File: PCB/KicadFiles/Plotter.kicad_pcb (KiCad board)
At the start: 2 copper layers, 1 part, among them U1 TMC2209-V1.2_Bigtreetech

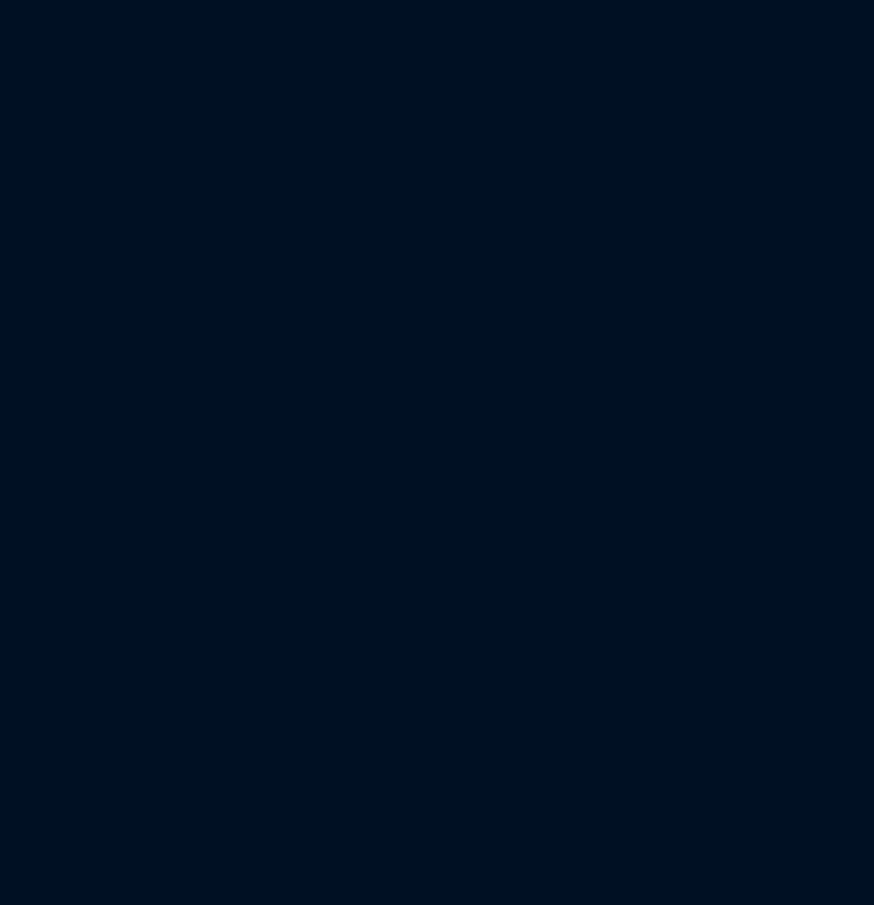
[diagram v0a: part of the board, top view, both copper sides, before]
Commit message: stall detect lauft
https://github.com/teemuatlut/TMCStepper/issues/178
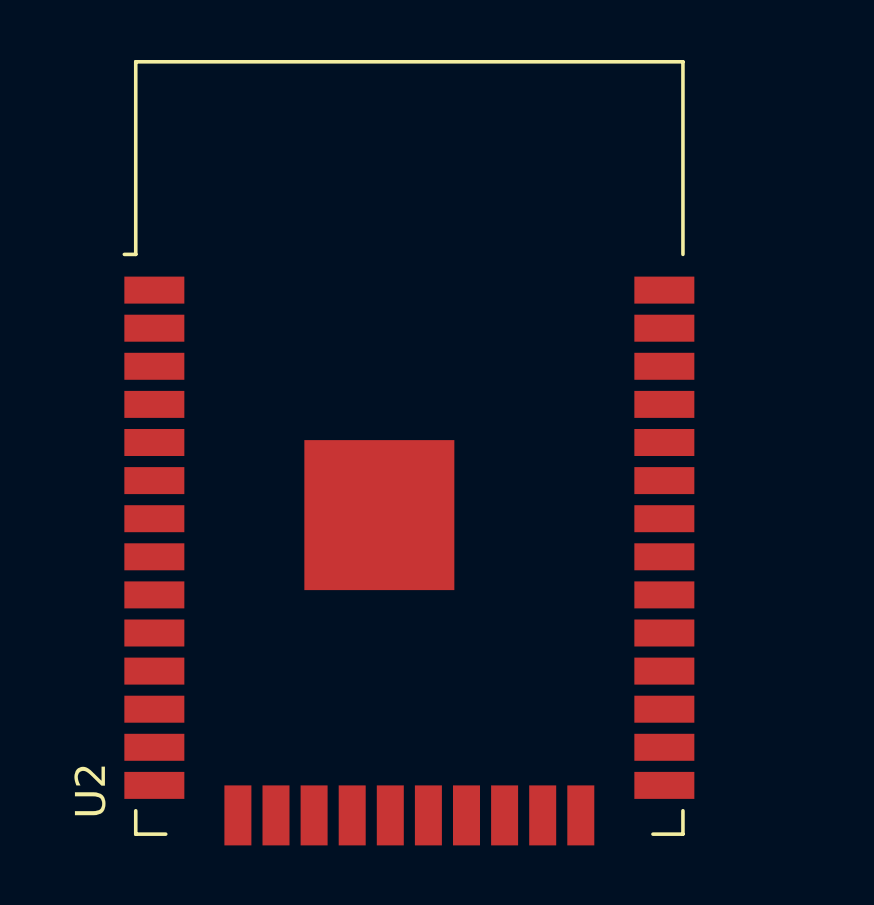
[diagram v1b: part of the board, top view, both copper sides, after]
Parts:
- added U2: ESP32-WROOM-32, RF_Module:ESP32-WROOM-32, F.Cu at (40.0, 70.0)

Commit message: schematic half way done
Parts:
- added C1: 100u, Capacitor_SMD:CP_Elec_6.3x7.7, F.Cu at (125.0, 65.0)
- added C2: 100u, Capacitor_SMD:CP_Elec_6.3x7.7, F.Cu at (131.2, 56.8)
- added C3: 100u, Capacitor_SMD:CP_Elec_6.3x7.7, F.Cu at (99.9, 96.2)
- added C4: C, Capacitor_SMD:C_0603_1608Metric, F.Cu at (87.7, 101.1)
- added C5: C, Capacitor_SMD:C_0603_1608Metric, F.Cu at (138.4, 59.5)
- added C6: 100u, Capacitor_SMD:CP_Elec_6.3x7.7, F.Cu at (143.1, 49.0)
- added D1: LED, LED_SMD:LED_0603_1608Metric, F.Cu at (138.4, 54.3)
- added D2: 10v, Package_TO_SOT_SMD:SOT-23, F.Cu at (111.6, 63.1)
- added D3: LED, LED_SMD:LED_0603_1608Metric, F.Cu at (138.4, 56.9)
- added D4: LED, LED_SMD:LED_0603_1608Metric, F.Cu at (116.1, 62.2)
- added D5: LED, LED_SMD:LED_0603_1608Metric, F.Cu at (116.1, 64.8)
- added F1: Fuse, Fuse:Fuseholder_Cylinder-5x20mm_Schurter_0031_8201_Horizontal_Open, F.Cu at (52.6, 85.6)
- added H1: MountingHole M3, MountingHole:MountingHole_3.2mm_M3_Pad_Via, F.Cu at (134.2, 64.8)
- added H2: MountingHole M3, MountingHole:MountingHole_3.2mm_M3_Pad_Via, F.Cu at (131.7, 73.0)
- added H3: MountingHole M3, MountingHole:MountingHole_3.2mm_M3_Pad_Via, F.Cu at (152.3, 48.9)
- added H4: MountingHole M3, MountingHole:MountingHole_3.2mm_M3_Pad_Via, F.Cu at (123.8, 73.0)
- added J1: JTAG, Connector_IDC:IDC-Header_2x10_P2.54mm_Vertical, F.Cu at (55.6, 51.0)
- added J2: DBG_UART, Connector_JST:JST_XH_B3B-XH-A_1x03_P2.50mm_Vertical, F.Cu at (68.2, 94.5)
- added J3: 12V IN, Connector_BarrelJack:BarrelJack_CLIFF_FC681465S_SMT_Horizontal, F.Cu at (118.2, 52.9)
- added J4: Motor LIN, Connector_JST:JST_XH_B4B-XH-A_1x04_P2.50mm_Vertical, F.Cu at (53.8, 94.5)
- added J5: Servo, Connector_JST:JST_XH_B3B-XH-A_1x03_P2.50mm_Vertical, F.Cu at (129.4, 48.2)
- added J6: Motor ROT, Connector_JST:JST_XH_B4B-XH-A_1x04_P2.50mm_Vertical, F.Cu at (95.3, 70.7)
- added Q1: SQJ479EP, Package_TO_SOT_SMD:TDSON-8-1, F.Cu at (54.4, 102.3)
- added R1: 100, Resistor_SMD:R_0603_1608Metric, F.Cu at (83.7, 101.1)
- added R10: 10k, Resistor_SMD:R_0603_1608Metric, F.Cu at (91.7, 103.6)
- added R11: 10k, Resistor_SMD:R_0603_1608Metric, F.Cu at (75.7, 104.1)
- added R12: 10k, Resistor_SMD:R_0603_1608Metric, F.Cu at (72.3, 78.7)
- added R13: 10k, Resistor_SMD:R_0603_1608Metric, F.Cu at (117.8, 78.3)
- added R14: R, Resistor_SMD:R_0603_1608Metric, F.Cu at (79.7, 103.6)
- added R15: 10k, Resistor_SMD:R_0603_1608Metric, F.Cu at (68.3, 78.7)
- added R16: 10k, Resistor_SMD:R_0603_1608Metric, F.Cu at (64.3, 78.7)
- added R17: R, Resistor_SMD:R_0603_1608Metric, F.Cu at (79.7, 101.1)
- added R18: 10k, Resistor_SMD:R_0603_1608Metric, F.Cu at (83.7, 103.6)
- added R19: 10k, Resistor_SMD:R_0603_1608Metric, F.Cu at (142.4, 56.8)
- added R2: 100, Resistor_SMD:R_0603_1608Metric, F.Cu at (107.2, 94.7)
- added R20: R, Resistor_SMD:R_0603_1608Metric, F.Cu at (95.7, 104.1)
- added R3: 100, Resistor_SMD:R_0603_1608Metric, F.Cu at (75.7, 101.6)
- added R4: 100, Resistor_SMD:R_0603_1608Metric, F.Cu at (142.4, 54.3)
- added R5: 100, Resistor_SMD:R_0603_1608Metric, F.Cu at (95.7, 101.6)
- added R6: 100, Resistor_SMD:R_0603_1608Metric, F.Cu at (121.8, 78.3)
- added R7: 100, Resistor_SMD:R_0603_1608Metric, F.Cu at (87.7, 103.6)
- added R8: R, Resistor_SMD:R_0603_1608Metric, F.Cu at (117.8, 80.8)
- added R9: 10k, Resistor_SMD:R_0603_1608Metric, F.Cu at (91.7, 101.1)
- added SW1: SW_Push, Button_Switch_THT:SW_PUSH_6mm_H5mm, F.Cu at (96.7, 77.1)
- added SW2: SW_Push, Button_Switch_THT:SW_PUSH_6mm_H5mm, F.Cu at (107.3, 78.7)
- added SW3: SW_Push, Button_Switch_THT:SW_PUSH_6mm_H5mm, F.Cu at (96.7, 85.7)
- added SW4: SW_Push, Button_Switch_THT:SW_PUSH_6mm_H5mm, F.Cu at (120.0, 85.0)
- added TP1: +12V, TestPoint:TestPoint_Loop_D2.54mm_Drill1.5mm_Beaded, F.Cu at (61.0, 102.3)
- added TP2: +5V, TestPoint:TestPoint_Loop_D2.54mm_Drill1.5mm_Beaded, F.Cu at (71.2, 101.5)
- added TP3: +3.3V, TestPoint:TestPoint_Loop_D2.54mm_Drill1.5mm_Beaded, F.Cu at (66.1, 101.5)
- added U3: AMS1117-3.3, Package_TO_SOT_SMD:SOT-223-3_TabPin2, F.Cu at (110.2, 89.3)
- added U4: TSR_1-2450, Converter_DCDC:Converter_DCDC_TRACO_TSR-1_THT, F.Cu at (110.6, 73.7)
- added U5: TMC2209-V1.2_Bigtreetech, Footprints:TMC2209-V1.2 Bigtreetech, F.Cu at (86.0, 88.7)
- U1: value TMC2209-V1.2_Bigtreetech -> ESP32-WROOM-32; footprint Footprints:TMC2209-V1.2 Bigtreetech -> RF_Module:ESP32-WROOM-32
- U2: value ESP32-WROOM-32 -> TMC2209-V1.2_Bigtreetech; footprint RF_Module:ESP32-WROOM-32 -> Footprints:TMC2209-V1.2 Bigtreetech
- moved U2 62.1 mm to (100.5, 56.2)
- moved U1 8.71 mm to (77.1, 66.4)
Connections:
- U1 pad 1: unconnected-(U1-Pad1) -> GND
- U1 pad 13: unconnected-(U1-Pad13) -> TMS
- U1 pad 14: unconnected-(U1-Pad14) -> TDI
- U1 pad 15: unconnected-(U1-Pad15) -> GND
- U1 pad 16: unconnected-(U1-Pad16) -> TCK
- U1 pad 2: unconnected-(U1-Pad2) -> +3.3V
- U2 pad 1: Net-(U2-Pad1) -> MOT_EN
- U2 pad 10: unconnected-(U2-Pad10) -> +3.3V
- U2 pad 11: unconnected-(U2-Pad11) -> Net-(J4-Pad4)
- U2 pad 12: unconnected-(U2-Pad12) -> Net-(J4-Pad3)
- U2 pad 13: unconnected-(U2-Pad13) -> Net-(J4-Pad2)
- U2 pad 14: unconnected-(U2-Pad14) -> Net-(J4-Pad1)
- U2 pad 15: Net-(U2-Pad1) -> GND
- U2 pad 16: unconnected-(U2-Pad16) -> +12V
- U2 pad 17: unconnected-(U2-Pad17) -> MOT_LIN_DIAG
- U2 pad 2: unconnected-(U2-Pad2) -> Net-(R10-Pad1)
- U2 pad 3: unconnected-(U2-Pad3) -> Net-(R11-Pad2)
- U2 pad 4: unconnected-(U2-Pad4) -> MOT_UART
- U2 pad 5: unconnected-(U2-Pad5) -> MOT_UART
- U2 pad 7: unconnected-(U2-Pad7) -> MOT_LIN_STEP
- U2 pad 8: unconnected-(U2-Pad8) -> MOT_LIN_DIR
- U2 pad 9: unconnected-(U2-Pad9) -> GND

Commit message: finished schematic
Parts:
- removed D5: LED, LED_SMD:LED_0603_1608Metric
- added C10: 100u, Capacitor_SMD:CP_Elec_6.3x7.7, F.Cu at (151.3, 116.9)
- added C7: 100n, Capacitor_SMD:C_0603_1608Metric, F.Cu at (198.9, 77.3)
- added C8: 100n, Capacitor_SMD:C_0603_1608Metric, F.Cu at (163.9, 105.3)
- added C9: 100u, Capacitor_SMD:CP_Elec_6.3x7.7, F.Cu at (156.7, 107.5)
- added R21: 100, Resistor_SMD:R_0603_1608Metric, F.Cu at (125.7, 133.4)
- added R22: 1k, Resistor_SMD:R_0603_1608Metric, F.Cu at (191.8, 85.5)
- added R23: 10k, Resistor_SMD:R_0603_1608Metric, F.Cu at (150.0, 84.1)
- added R24: 1k, Resistor_SMD:R_0603_1608Metric, F.Cu at (145.8, 132.8)
- added R25: 10k, Resistor_SMD:R_0603_1608Metric, F.Cu at (202.9, 74.2)
- added R26: 1k, Resistor_SMD:R_0603_1608Metric, F.Cu at (210.0, 66.2)
- added R27: 10k, Resistor_SMD:R_0603_1608Metric, F.Cu at (187.8, 88.0)
- added R28: 1k, Resistor_SMD:R_0603_1608Metric, F.Cu at (177.2, 97.9)
- added R29: 10k, Resistor_SMD:R_0603_1608Metric, F.Cu at (177.2, 100.4)
- added R30: 10k, Resistor_SMD:R_0603_1608Metric, F.Cu at (137.7, 133.4)
- added R31: 10k, Resistor_SMD:R_0603_1608Metric, F.Cu at (150.8, 127.2)
- added R32: 10k, Resistor_SMD:R_0603_1608Metric, F.Cu at (144.0, 99.8)
- added R33: 10k, Resistor_SMD:R_0603_1608Metric, F.Cu at (202.9, 76.7)
- added R34: 10k, Resistor_SMD:R_0603_1608Metric, F.Cu at (133.7, 133.4)
- added R35: 10k, Resistor_SMD:R_0603_1608Metric, F.Cu at (144.0, 114.1)
- added R36: 10k, Resistor_SMD:R_0603_1608Metric, F.Cu at (189.3, 90.6)
- added R37: 10k, Resistor_SMD:R_0603_1608Metric, F.Cu at (166.5, 110.3)
- added U6: TMC2209-V1.2_Bigtreetech, Footprints:TMC2209-V1.2 Bigtreetech, F.Cu at (166.4, 76.3)
- added U7: TMC2209-V1.2_Bigtreetech, Footprints:TMC2209-V1.2 Bigtreetech, F.Cu at (139.3, 87.4)
- C2, C3: value 100u -> C; footprint Capacitor_SMD:CP_Elec_6.3x7.7 -> Capacitor_SMD:C_0603_1608Metric
- C4: value C -> 100u; footprint Capacitor_SMD:C_0603_1608Metric -> Capacitor_SMD:CP_Elec_6.3x7.7
- C5: value C -> 100n
- C6: value 100u -> 100n; footprint Capacitor_SMD:CP_Elec_6.3x7.7 -> Capacitor_SMD:C_0603_1608Metric
- D1: value LED -> 10v; footprint LED_SMD:LED_0603_1608Metric -> Package_TO_SOT_SMD:SOT-23
- D2: value 10v -> LED; footprint Package_TO_SOT_SMD:SOT-23 -> LED_SMD:LED_0603_1608Metric
- J1: value JTAG -> 12V IN; footprint Connector_IDC:IDC-Header_2x10_P2.54mm_Vertical -> Connector_BarrelJack:BarrelJack_CLIFF_FC681465S_SMT_Horizontal
- J2: value DBG_UART -> JTAG; footprint Connector_JST:JST_XH_B3B-XH-A_1x03_P2.50mm_Vertical -> Connector_IDC:IDC-Header_2x10_P2.54mm_Vertical
- J3: value 12V IN -> DBG_UART; footprint Connector_BarrelJack:BarrelJack_CLIFF_FC681465S_SMT_Horizontal -> Connector_JST:JST_XH_B3B-XH-A_1x03_P2.50mm_Vertical
- J4: value Motor LIN -> Servo; footprint Connector_JST:JST_XH_B4B-XH-A_1x04_P2.50mm_Vertical -> Connector_JST:JST_XH_B3B-XH-A_1x03_P2.50mm_Vertical
- J5: value Servo -> Motor LIN; footprint Connector_JST:JST_XH_B3B-XH-A_1x03_P2.50mm_Vertical -> Connector_JST:JST_XH_B4B-XH-A_1x04_P2.50mm_Vertical
- R1, R6, R7: value 100 -> 10k
- R10, R11, R12, R13, R15, R16, R18, R19: value 10k -> 100
- R14, R20: value R -> 100
- R17: value R -> 1k
- R2, R3, R4: value 100 -> R
- R5: value 100 -> 1k
- R8: value R -> 3k
- R9: value 10k -> 3k
- SW1: value SW_Push -> Down
- SW2: value SW_Push -> Up
- SW3: value SW_Push -> Enter
- SW4: value SW_Push -> RST
- U1: value ESP32-WROOM-32 -> TSR_1-2450; footprint RF_Module:ESP32-WROOM-32 -> Converter_DCDC:Converter_DCDC_TRACO_TSR-1_THT
- U2: value TMC2209-V1.2_Bigtreetech -> AMS1117-3.3; footprint Footprints:TMC2209-V1.2 Bigtreetech -> Package_TO_SOT_SMD:SOT-223-3_TabPin2
- U3: value AMS1117-3.3 -> ESP32-WROOM-32; footprint Package_TO_SOT_SMD:SOT-223-3_TabPin2 -> RF_Module:ESP32-WROOM-32
- U4: value TSR_1-2450 -> MicroSD; footprint Converter_DCDC:Converter_DCDC_TRACO_TSR-1_THT -> Footprints:GCT-MEM2055-00-190-01-A
- U5: value TMC2209-V1.2_Bigtreetech -> OLED_Display; footprint Footprints:TMC2209-V1.2 Bigtreetech -> Footprints:Display_128x64_096_I2C
- moved R7 114.8 mm to (198.9, 74.8)
- moved R3 113.6 mm to (187.8, 83.0)
- moved J1 110.8 mm to (157.1, 95.4)
- moved R16 107.6 mm to (167.9, 107.8)
- moved R15 103.1 mm to (167.9, 105.3)
- moved R10 102.2 mm to (191.8, 83.0)
- moved R18 102.1 mm to (185.3, 93.1)
- moved R17 101.6 mm to (181.2, 97.9)
- moved Q1 100.3 mm to (152.1, 79.5)
- moved R11 96.3 mm to (171.9, 107.8)
- moved C4 94.3 mm to (180.6, 84.7)
- moved U2 93.9 mm to (191.9, 77.7)
- moved R8 93.0 mm to (210.0, 68.7)
- moved R2 92.9 mm to (198.9, 79.8)
- moved J4 87.4 mm to (137.6, 119.2)
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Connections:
- C1 pad 1: +12V -> +5V
- C3 pad 1: +12V -> +3.3V
- C4 pad 1: +5V -> +3.3V
- C5 pad 1: +3.3V -> SW_Down
- C6 pad 1: +3.3V -> SW_Up
- D1 pad 1: unconnected-(D1-Pad1) -> Net-(D1-Pad1)
- D2 pad 1: Net-(Q1-Pad4) -> GND
- D2 pad 2: unconnected-(D2-Pad2) -> Net-(D2-Pad2)
- D3 pad 2: Net-(R14-Pad2) -> Net-(D3-Pad2)
- D4 pad 2: Net-(R17-Pad2) -> Net-(D4-Pad2)
- J1 pad 1: +3.3V -> Net-(F1-Pad1)
- J1 pad 2: unconnected-(J1-Pad2) -> GND
- J1 pad 3: Net-(J1-Pad3) -> GND
- J2 pad 1: GND -> +3.3V
- J2 pad 2: Net-(J2-Pad2) -> unconnected-(J2-Pad2)
- J3 pad 1: Net-(F1-Pad1) -> GND
- J3 pad 2: GND -> Net-(J3-Pad2)
- J3 pad 3: GND -> Net-(J3-Pad3)
- J4 pad 1: Net-(J4-Pad1) -> GND
- J4 pad 2: Net-(J4-Pad2) -> +5V
- J5 pad 1: unconnected-(J5-Pad1) -> Net-(J5-Pad1)
- J5 pad 2: unconnected-(J5-Pad2) -> Net-(J5-Pad2)
- J5 pad 3: unconnected-(J5-Pad3) -> Net-(J5-Pad3)
- Q1 pad 4: Net-(Q1-Pad4) -> Net-(D1-Pad1)
- R1 pad 1: RST -> Net-(D1-Pad1)
- R1 pad 2: Net-(J1-Pad3) -> GND
- R10 pad 1: Net-(R10-Pad1) -> RST
- R10 pad 2: GND -> Net-(J2-Pad3)
- R11 pad 1: +3.3V -> JTAG_TDI
- R11 pad 2: Net-(R11-Pad2) -> Net-(J2-Pad5)
- R12 pad 1: Net-(R11-Pad2) -> JTAG_TMS
- R12 pad 2: GND -> Net-(J2-Pad7)
- R13 pad 1: Net-(Q1-Pad4) -> JTAG_TCK
- R13 pad 2: GND -> Net-(J2-Pad9)
- R14 pad 1: +5V -> JTAG_TDO
- R14 pad 2: Net-(R14-Pad2) -> Net-(J2-Pad13)
- R15 pad 1: +3.3V -> DEBUG_UART_TX
- R15 pad 2: Net-(R15-Pad2) -> Net-(J3-Pad3)
- R16 pad 1: Net-(R15-Pad2) -> DEBUG_UART_RX
- R16 pad 2: GND -> Net-(J3-Pad2)
- R17 pad 1: +3.3V -> Servo
- R17 pad 2: Net-(R17-Pad2) -> Net-(J4-Pad3)
- R18 pad 1: +3.3V -> SD_CE
- R19 pad 1: Net-(R18-Pad2) -> SD_MOSI
- R19 pad 2: GND -> Net-(R19-Pad2)
- R2 pad 1: TDI -> +12V
- R2 pad 2: Net-(J1-Pad5) -> Net-(D2-Pad2)
- R20 pad 1: +12V -> SD_SCK
- R20 pad 2: Net-(D5-Pad2) -> Net-(R20-Pad2)
- R3 pad 1: TMS -> +5V
- R3 pad 2: Net-(J1-Pad7) -> Net-(D3-Pad2)
- R4 pad 1: TCK -> +3.3V
- R4 pad 2: Net-(J1-Pad9) -> Net-(D4-Pad2)
- R5 pad 1: TDO -> MOT_UART
- R5 pad 2: Net-(J1-Pad13) -> Net-(R5-Pad2)
- R6 pad 1: DEBUG_UART_TX -> +3.3V
- R6 pad 2: Net-(J2-Pad3) -> Net-(R6-Pad2)
- R7 pad 1: DEBUG_UART_RX -> Net-(R6-Pad2)
- R7 pad 2: Net-(J2-Pad2) -> GND
- R8 pad 1: unconnected-(R8-Pad1) -> +3.3V
- R8 pad 2: unconnected-(R8-Pad2) -> SDA
- R9 pad 2: Net-(R10-Pad1) -> SCL
- SW1 pad 1: unconnected-(SW1-Pad1) -> GND
- SW1 pad 2: unconnected-(SW1-Pad2) -> Net-(R22-Pad1)
- SW2 pad 1: unconnected-(SW2-Pad1) -> GND
- SW2 pad 2: unconnected-(SW2-Pad2) -> Net-(R24-Pad1)
- SW3 pad 1: unconnected-(SW3-Pad1) -> GND
- SW3 pad 2: unconnected-(SW3-Pad2) -> Net-(R26-Pad1)
- SW4 pad 1: unconnected-(SW4-Pad1) -> GND
- SW4 pad 2: unconnected-(SW4-Pad2) -> Net-(R28-Pad1)
- U1 pad 1: GND -> +12V
- U1 pad 2: +3.3V -> GND
- U1 pad 3: unconnected-(U1-Pad3) -> +5V
- U2 pad 1: MOT_EN -> GND
- U2 pad 2: Net-(R10-Pad1) -> +3.3V
- U2 pad 3: Net-(R11-Pad2) -> +5V
- U3 pad 3: +5V -> RST
- U4 pad 1: +12V -> unconnected-(U4-Pad1)
- U4 pad 2: GND -> Net-(R18-Pad2)
- U4 pad 3: +5V -> Net-(R19-Pad2)
- U5 pad 1: MOT_EN -> GND
- U5 pad 2: Net-(R15-Pad2) -> +3.3V
- U5 pad 3: Net-(R18-Pad2) -> SCL
- U5 pad 4: MOT_UART -> SDA

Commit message: stm32??
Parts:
- added JP1: SolderJumper_3_Open, Jumper:SolderJumper-3_P1.3mm_Open_RoundedPad1.0x1.5mm, F.Cu at (254.0, -40.6)
- added U8: STM32F411CEUx, Package_DFN_QFN:QFN-48-1EP_7x7mm_P0.5mm_EP5.6x5.6mm, F.Cu at (256.5, -53.3)
- C2, C3, C5, C6, C7, C8: footprint Capacitor_SMD:C_0603_1608Metric -> Capacitor_SMD:C_0805_2012Metric
- D2, D3, D4: footprint LED_SMD:LED_0603_1608Metric -> LED_SMD:LED_0805_2012Metric
- R1, R10, R11, R12, R13, R14, R15, R16, R17, R18, R19, R2, R20, R21, R22, R23, R24, R25, R26, R27, R28, R29, R3, R30, R31, R32, R33, R34, R35, R36, R37, R4, R5, R6, R7, R8, R9: footprint Resistor_SMD:R_0603_1608Metric -> Resistor_SMD:R_0805_2012Metric
- moved D4 269.7 mm to (347.7, -56.1)
- moved C3 253.8 mm to (332.7, -56.1)
- moved C2 245.9 mm to (327.7, -46.1)
- moved D3 234.7 mm to (327.7, -41.1)
- moved D1 231.6 mm to (302.7, -46.1)
- moved U1 224.3 mm to (312.7, -36.1)
- moved R1 223.8 mm to (307.7, -46.1)
- moved R8 220.9 mm to (10.0, -25.0)
- moved F1 219.1 mm to (312.7, -54.9), turned to 90 degrees
- moved D2 218.2 mm to (302.7, -36.1)
- moved R4 215.1 mm to (342.7, -56.1)
- moved SW2 210.4 mm to (271.1, -22.6)
- moved C1 208.3 mm to (327.7, -36.1)
- moved C4 207.6 mm to (337.7, -51.1)
- moved R7 207.0 mm to (10.0, -10.0)
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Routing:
- net unconnected-(JP1-Pad2): track 0.00 -> 2.54 mm
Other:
- board outline added: 78.7 x 81.3 mm
- copper layers 2 -> 4

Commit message: bald fertig
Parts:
- removed R30, R31, R32, R33, R34, R35, R36, R37: 10k, Resistor_SMD:R_0805_2012Metric
- removed TP1: +12V, TestPoint:TestPoint_Loop_D2.54mm_Drill1.5mm_Beaded
- removed TP2: +5V, TestPoint:TestPoint_Loop_D2.54mm_Drill1.5mm_Beaded
- removed TP3: +3.3V, TestPoint:TestPoint_Loop_D2.54mm_Drill1.5mm_Beaded
- removed U8: STM32F411CEUx, Package_DFN_QFN:QFN-48-1EP_7x7mm_P0.5mm_EP5.6x5.6mm
- added C11: 12p, Capacitor_SMD:C_0402_1005Metric, F.Cu at (84.0, 113.5)
- added C12: 100n, Capacitor_SMD:C_0805_2012Metric, F.Cu at (123.5, 136.5)
- added C13: 100n, Capacitor_SMD:C_0805_2012Metric, F.Cu at (123.5, 123.5)
- added C14: 100n, Capacitor_SMD:C_0805_2012Metric, F.Cu at (123.5, 130.0)
- added C15: 100n, Capacitor_SMD:C_0805_2012Metric, F.Cu at (104.0, 108.0)
- added C16: 100n, Capacitor_SMD:C_0805_2012Metric, F.Cu at (66.0, 70.5)
- added C17: 100u, Capacitor_SMD:CP_Elec_6.3x7.7, F.Cu at (78.3, 73.5)
- added C18: 100u, Capacitor_SMD:CP_Elec_6.3x7.7, F.Cu at (55.5, 73.5)
- added D5: Status, LED_SMD:LED_0805_2012Metric, F.Cu at (121.5, 118.5)
- added JP2: Y_MS1, Jumper:SolderJumper-3_P1.3mm_Open_RoundedPad1.0x1.5mm, F.Cu at (53.7, 96.5)
- added JP3: X_MS2, Jumper:SolderJumper-3_P1.3mm_Open_RoundedPad1.0x1.5mm, F.Cu at (82.0, 96.0)
- added JP4: Y_MS2, Jumper:SolderJumper-3_P1.3mm_Open_RoundedPad1.0x1.5mm, F.Cu at (58.7, 96.5)
- added Y1: 25MHz, Crystal:Crystal_SMD_3225-4Pin_3.2x2.5mm, F.Cu at (86.4, 114.5)
- C10: value 100u -> 12p; footprint Capacitor_SMD:CP_Elec_6.3x7.7 -> Capacitor_SMD:C_0402_1005Metric
- C2, C3: value C -> 10u
- C5: value 100n -> 2.2u; footprint Capacitor_SMD:C_0805_2012Metric -> Capacitor_SMD:C_0402_1005Metric
- C6, C7, C8: footprint Capacitor_SMD:C_0805_2012Metric -> Capacitor_SMD:C_0402_1005Metric
- C9: value 100u -> 100n; footprint Capacitor_SMD:CP_Elec_6.3x7.7 -> Capacitor_SMD:C_0402_1005Metric
- D2: value LED -> 12V
- D3: value LED -> 5V
- D4: value LED -> 3.3V
- J1: value 12V IN -> 12V Input; footprint Connector_BarrelJack:BarrelJack_CLIFF_FC681465S_SMT_Horizontal -> Connector_JST:JST_XH_B2B-XH-A_1x02_P2.50mm_Vertical
- J3: value DBG_UART -> Servo
- J4: value Servo -> Ext. Switch; footprint Connector_JST:JST_XH_B3B-XH-A_1x03_P2.50mm_Vertical -> Connector_JST:JST_XH_B2B-XH-A_1x02_P2.50mm_Vertical
- J5: value Motor LIN -> Motor X
- J6: value Motor ROT -> Motor Y
- JP1: value SolderJumper_3_Open -> X_MS1
- R10, R11, R13, R15: value 100 -> 1k
- R12, R14, R16, R18: value 100 -> 10k
- R2, R3, R4: value R -> 1k
- R22, R26, R28: value 1k -> 100
- R23, R25, R27, R29: value 10k -> 100
- R24, R5: value 1k -> 10k
- R6, R7: value 10k -> 3k
- R8: value 3k -> 10k
- R9: value 3k -> 1k
- SW3: value Enter -> OK
- U3: value ESP32-WROOM-32 -> STM32F411CEU&; footprint RF_Module:ESP32-WROOM-32 -> Package_DFN_QFN:QFN-48-1EP_7x7mm_P0.5mm_EP5.6x5.6mm
- U4: value MicroSD -> OLED_Display; footprint Footprints:GCT-MEM2055-00-190-01-A -> Footprints:Display_128x64_096_I2C
- U5: value OLED_Display -> MicroSD; footprint Footprints:Display_128x64_096_I2C -> Footprints:GCT-MEM2055-00-190-01-A
- moved R4 285.5 mm to (114.9, 116.0)
- moved D4 284.2 mm to (121.5, 116.0), turned to 180 degrees
- moved C4 279.8 mm to (101.5, 99.0), turned to 180 degrees
- moved C3 263.3 mm to (115.0, 92.0), turned to 90 degrees
- moved U2 260.5 mm to (110.0, 92.0), turned to -90 degrees
- moved C1 259.7 mm to (99.5, 88.0), turned to -90 degrees
- moved R3 259.0 mm to (114.9, 113.5)
- moved D3 257.8 mm to (121.4, 113.5), turned to 180 degrees
- moved C2 254.6 mm to (110.0, 86.0)
- moved R26 242.3 mm to (69.5, 131.5), turned to -90 degrees
- moved R2 241.6 mm to (114.9, 111.0)
- moved U5 241.3 mm to (70.0, 133.9), turned to 180 degrees
- moved R27 239.8 mm to (67.5, 131.5), turned to -90 degrees
- moved R25 239.7 mm to (71.5, 131.5), turned to -90 degrees
- moved H3 239.2 mm to (54.0, 64.0)
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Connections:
- C10 pad 1: +12V -> Net-(C10-Pad1)
- C5 pad 1: SW_Down -> Net-(C5-Pad1)
- C6 pad 1: SW_Up -> +3.3V
- C7 pad 1: SW_Enter -> +3.3V
- C8 pad 1: RST -> +3.3V
- C9 pad 1: +12V -> +3.3V
- J1 pad 1: Net-(F1-Pad1) -> GND
- J1 pad 2: GND -> Net-(F1-Pad1)
- J2 pad 13: Net-(J2-Pad13) -> unconnected-(J2-Pad13)
- J2 pad 17: unconnected-(J2-Pad17) -> Net-(J2-Pad17)
- J2 pad 3: Net-(J2-Pad3) -> unconnected-(J2-Pad3)
- J3 pad 2: Net-(J3-Pad2) -> +5V
- J4 pad 2: +5V -> Ext. Switch
- JP1 pad 1: unconnected-(JP1-Pad1) -> GND
- JP1 pad 2: unconnected-(JP1-Pad2) -> Net-(JP1-Pad2)
- JP1 pad 3: unconnected-(JP1-Pad3) -> +3.3V
- R10 pad 1: RST -> Net-(R10-Pad1)
- R10 pad 2: Net-(J2-Pad3) -> MOT_UART
- R11 pad 1: JTAG_TDI -> Net-(R11-Pad1)
- R11 pad 2: Net-(J2-Pad5) -> SW_Down
- R12 pad 1: JTAG_TMS -> +3.3V
- R12 pad 2: Net-(J2-Pad7) -> SW_Down
- R13 pad 1: JTAG_TCK -> Net-(R13-Pad1)
- R13 pad 2: Net-(J2-Pad9) -> SW_Up
- R14 pad 1: JTAG_TDO -> +3.3V
- R14 pad 2: Net-(J2-Pad13) -> SW_Up
- R15 pad 1: DEBUG_UART_TX -> Net-(R15-Pad1)
- R15 pad 2: Net-(J3-Pad3) -> SW_OK
- R16 pad 1: DEBUG_UART_RX -> +3.3V
- R16 pad 2: Net-(J3-Pad2) -> SW_OK
- R17 pad 1: Servo -> Net-(R17-Pad1)
- R17 pad 2: Net-(J4-Pad3) -> RST
- R18 pad 1: SD_CE -> +3.3V
- R18 pad 2: Net-(R18-Pad2) -> RST
- R19 pad 1: SD_MOSI -> PC_UART_RX
- R19 pad 2: Net-(R19-Pad2) -> Net-(J2-Pad5)
- R20 pad 1: SD_SCK -> SWD_SWDIO
- R20 pad 2: Net-(R20-Pad2) -> Net-(J2-Pad7)
- R21 pad 1: SD_MISO -> SWD_SWCLK
- R21 pad 2: Net-(R21-Pad2) -> Net-(J2-Pad9)
- R22 pad 1: Net-(R22-Pad1) -> PC_UART_TX
- R22 pad 2: SW_Down -> Net-(J2-Pad17)
- R23 pad 1: +3.3V -> Servo
- R23 pad 2: SW_Down -> Net-(J3-Pad3)
- R24 pad 1: Net-(R24-Pad1) -> Ext. Switch
- R24 pad 2: SW_Up -> +3.3V
- R25 pad 1: +3.3V -> SD_CE
- R25 pad 2: SW_Up -> Net-(R25-Pad2)
- R26 pad 1: Net-(R26-Pad1) -> SD_MOSI
- R26 pad 2: SW_Enter -> Net-(R26-Pad2)
- R27 pad 1: +3.3V -> SD_SCK
- R27 pad 2: SW_Enter -> Net-(R27-Pad2)
- R28 pad 1: Net-(R28-Pad1) -> SD_DETECT
- R28 pad 2: RST -> Net-(R28-Pad2)
- R29 pad 1: +3.3V -> SD_MISO
- R29 pad 2: RST -> Net-(R29-Pad2)
- R5 pad 1: MOT_UART -> GND
- R6 pad 2: Net-(R6-Pad2) -> I2C_SCL
- R7 pad 1: Net-(R6-Pad2) -> +3.3V
- R7 pad 2: GND -> I2C_SDA
- R8 pad 1: +3.3V -> GND
- R8 pad 2: SDA -> Net-(R8-Pad2)
- R9 pad 1: +3.3V -> Net-(D5-Pad2)
- R9 pad 2: SCL -> Net-(R9-Pad2)
- SW1 pad 2: Net-(R22-Pad1) -> Net-(R11-Pad1)
- SW2 pad 2: Net-(R24-Pad1) -> Net-(R13-Pad1)
- SW3 pad 2: Net-(R26-Pad1) -> Net-(R15-Pad1)
- SW4 pad 2: Net-(R28-Pad1) -> Net-(R17-Pad1)
- U3 pad 1: GND -> +3.3V
- U3 pad 10: MOT_ROT_DIAG -> unconnected-(U3-Pad10)
- U3 pad 11: MOT_LIN_DIAG -> SD_MOSI
- U3 pad 12: MOT_LIN_STEP -> Net-(R10-Pad1)
- U3 pad 13: JTAG_TMS -> MOT_UART
- U3 pad 14: JTAG_TDI -> Ext. Switch
- U3 pad 15: GND -> MOT_X_DIR
- U3 pad 16: JTAG_TCK -> MOT_X_STEP
- U3 pad 17: unconnected-(U3-Pad17) -> MOT_EN
- U3 pad 18: unconnected-(U3-Pad18) -> MOT_X_DIAG
- U3 pad 2: +3.3V -> Net-(R9-Pad2)
- U3 pad 20: unconnected-(U3-Pad20) -> Net-(R8-Pad2)
- U3 pad 22: unconnected-(U3-Pad22) -> Net-(C5-Pad1)
- U3 pad 23: JTAG_TDO -> GND
- U3 pad 24: SW_Down -> +3.3V
- U3 pad 25: Net-(R6-Pad2) -> MOT_Y_DIR
- U3 pad 26: SD_CE -> SD_SCK
- U3 pad 27: MOT_UART -> MOT_Y_STEP
- U3 pad 28: Net-(R5-Pad2) -> MOT_Y_DIAG
- U3 pad 29: SD_SCK -> Servo
- U3 pad 3: RST -> unconnected-(U3-Pad3)
- U3 pad 30: SD_MOSI -> PC_UART_TX
- U3 pad 31: SD_MISO -> PC_UART_RX
- U3 pad 32: unconnected-(U3-Pad32) -> SD_MISO
- U3 pad 33: Servo -> unconnected-(U3-Pad33)
- U3 pad 34: DEBUG_UART_RX -> SWD_SWDIO
- U3 pad 35: DEBUG_UART_TX -> GND
- U3 pad 36: SCL -> +3.3V
- U3 pad 37: SDA -> SWD_SWCLK
- U3 pad 38: GND -> SD_DETECT
- U3 pad 39: GND -> SD_CE
- U3 pad 4: SW_Up -> unconnected-(U3-Pad4)
- U3 pad 5: SW_Enter -> Net-(C10-Pad1)
- U3 pad 6: MOT_ROT_DIR -> Net-(C11-Pad1)
- U3 pad 7: MOT_EN -> RST
- U3 pad 8: MOT_LIN_DIR -> GND
- U3 pad 9: MOT_ROT_STEP -> +3.3V
- U4 pad 1: unconnected-(U4-Pad1) -> GND
- U4 pad 2: Net-(R18-Pad2) -> +3.3V
- U4 pad 3: Net-(R19-Pad2) -> I2C_SCL
- U4 pad 4: +3.3V -> I2C_SDA
- U5 pad 1: GND -> unconnected-(U5-Pad1)
- U5 pad 2: +3.3V -> Net-(R25-Pad2)
- U5 pad 3: SCL -> Net-(R26-Pad2)
- U5 pad 4: SDA -> +3.3V
- U6 pad 17: MOT_LIN_DIAG -> MOT_X_DIAG
- U6 pad 2: Net-(R30-Pad2) -> Net-(JP1-Pad2)
- U6 pad 7: MOT_LIN_STEP -> MOT_X_STEP
- U6 pad 8: MOT_LIN_DIR -> MOT_X_DIR
- U7 pad 17: MOT_ROT_DIAG -> MOT_Y_DIAG
- U7 pad 7: MOT_ROT_STEP -> MOT_Y_STEP
- U7 pad 8: MOT_ROT_DIR -> MOT_Y_DIR
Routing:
- net +3.3V: track 0.00 -> 156.6 mm, vias 0 -> 19
- net +12V: track 0.00 -> 154.6 mm
- net +5V: track 0.00 -> 122.2 mm
- net Ext. Switch: track 0.00 -> 72.2 mm, vias 0 -> 1
- net Servo: track 0.00 -> 70.4 mm, vias 0 -> 2
- net SW_Down: track 0.00 -> 67.2 mm
- net SW_OK: track 0.00 -> 63.7 mm
- net SW_Up: track 0.00 -> 61.7 mm, vias 0 -> 2
- net MOT_UART: track 0.00 -> 54.0 mm, vias 0 -> 2
- net GND: track 0.00 -> 51.4 mm, vias 0 -> 19
- net MOT_EN: track 0.00 -> 43.4 mm
- net MOT_Y_DIAG: track 0.00 -> 42.2 mm
- net Net-(R9-Pad2): track 0.00 -> 37.6 mm
- net SD_MOSI: track 0.00 -> 29.2 mm, vias 0 -> 2
- net RST: track 0.00 -> 29.1 mm
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- added copper zone on B.Cu, net GND
- added copper zone on F.Cu, net GND
- added copper zone on In1.Cu, net GND
- added copper zone on In2.Cu, net GND
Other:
- board size 78.7 x 81.3 mm -> 80 x 90 mm
- board text added: "+"
